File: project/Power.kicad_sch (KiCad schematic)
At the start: 20 parts, among them IC101 nPM1300-QEXX, X101 BATTERY

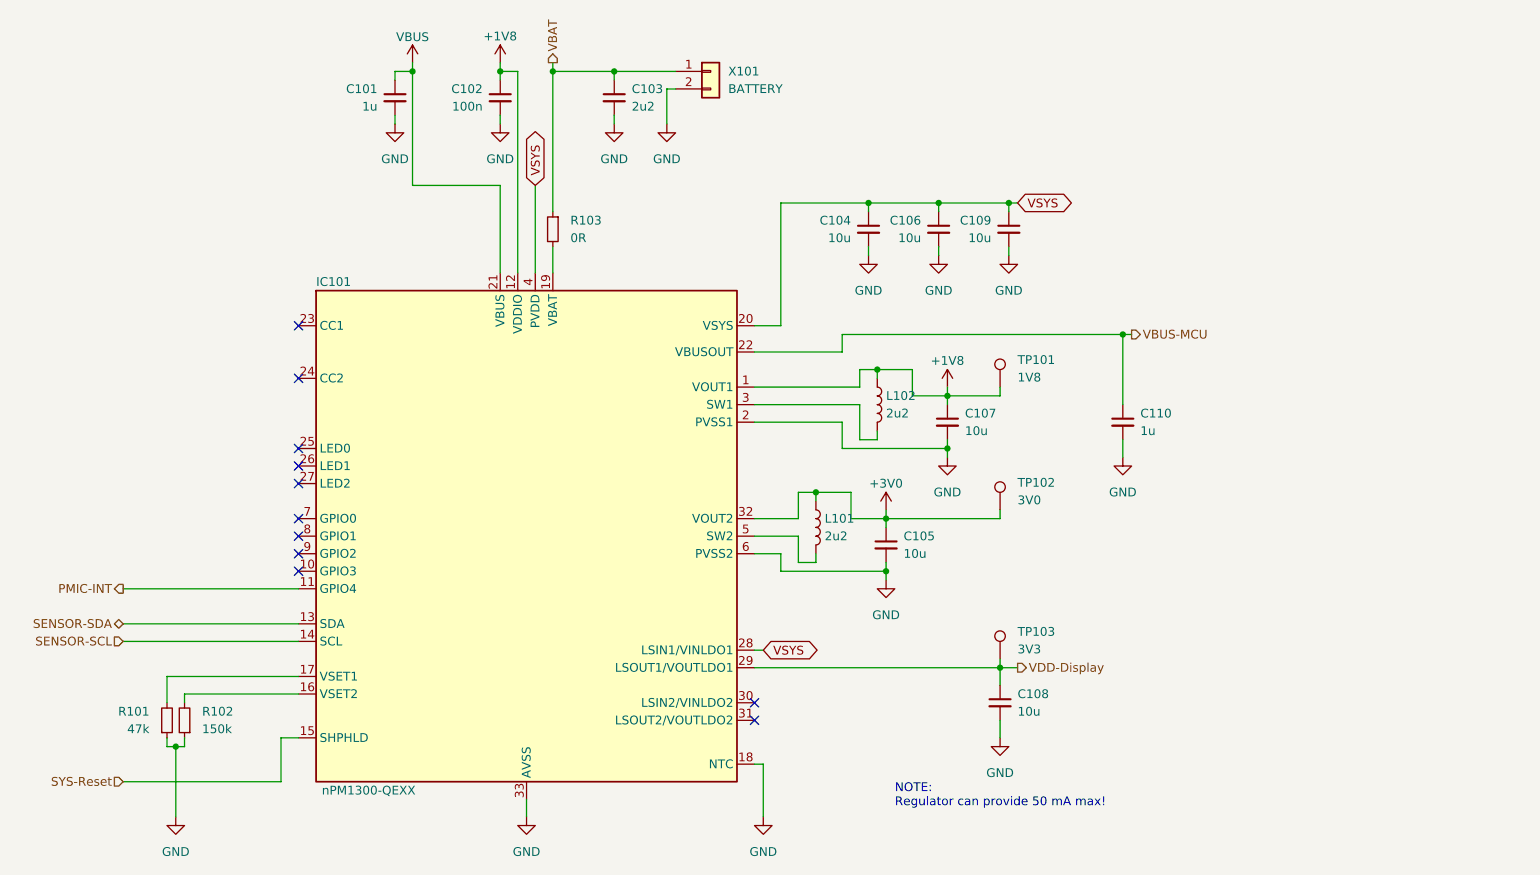
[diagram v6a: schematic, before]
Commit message: Update library paths, fix wrong supply voltage for vibration motor (VSys instead VBusOut)
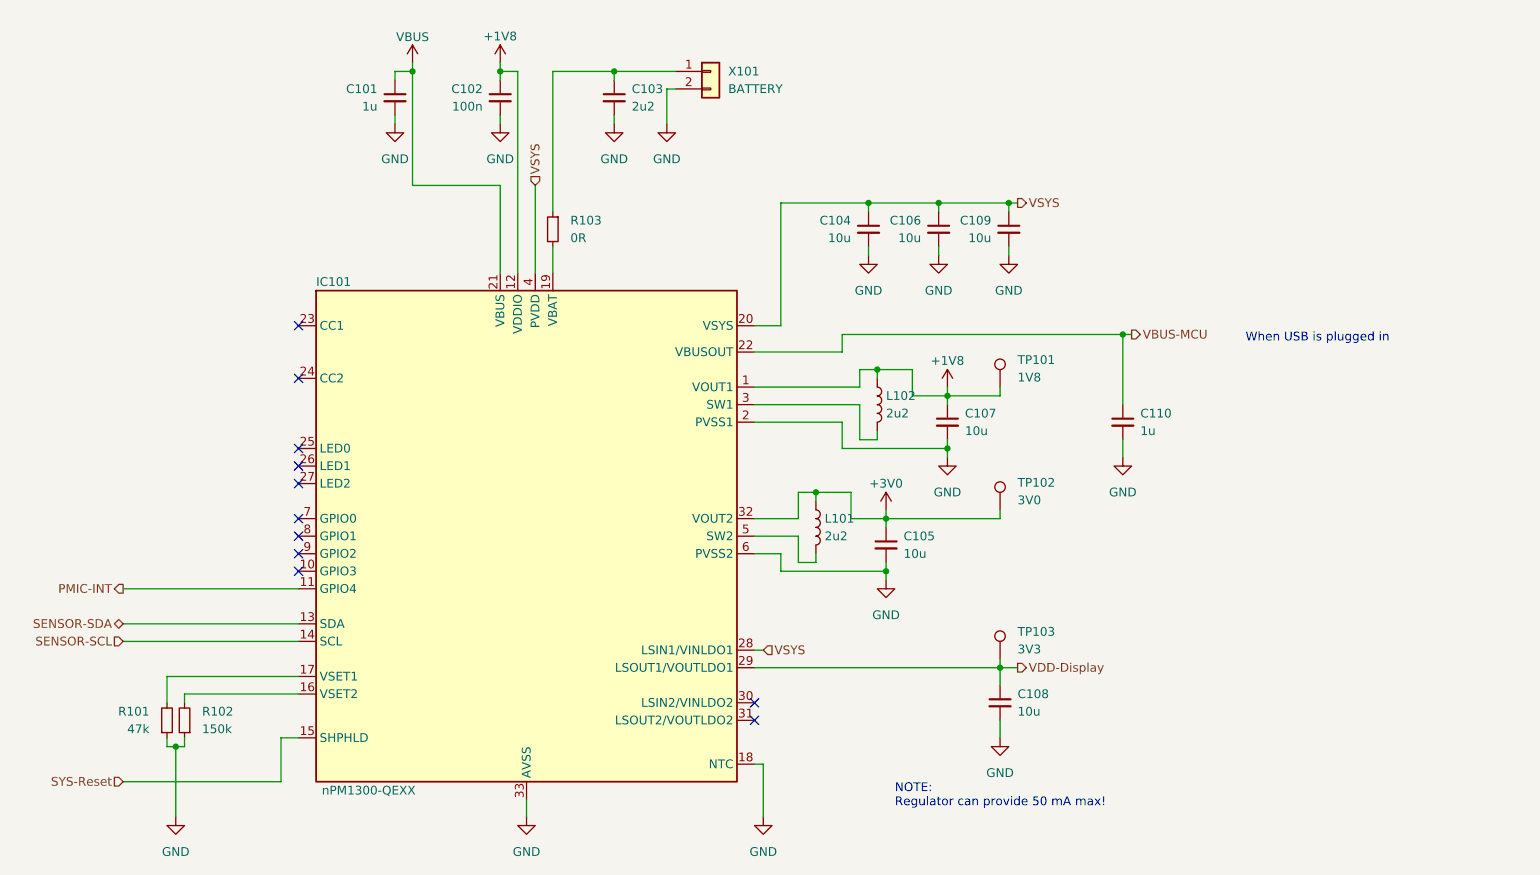
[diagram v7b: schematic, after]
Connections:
- net VBAT: no longer names the net of C103.1, R103.1, X101.1 (Pin_1)
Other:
- note added: "When USB is plugged in"
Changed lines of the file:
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@@
   (junction (at 181.61 59.69) (diameter 0) (color 0 0 0 0)
-  )
-  (junction (at 135.89 40.64) (diameter 0) (color 0 0 0 0)
   )
   (junction (at 182.88 83.82) (diameter 0) (color 0 0 0 0)
@@
     (stroke (width 0) (type default))
   )
-  (wire (pts (xy 135.89 39.37) (xy 135.89 40.64))
-    (stroke (width 0) (type default))
-  )
   (wire (pts (xy 182.88 83.82) (xy 187.96 83.82))
     (stroke (width 0) (type default))
@@
   (wire (pts (xy 133.35 69.85) (xy 133.35 57.15))
     (stroke (width 0) (type default))
+  )
+  (text "When USB is plugged in" (at 236.22 80.01 0)
+    (effects (font (size 1.27 1.27)) (justify left bottom))
   )
   (text "NOTE:\nRegulator can provide 50 mA max!" (at 185.42 147.32 0)
     (effects (font (size 1.27 1.27)) (justify left bottom))
   )
-  (global_label "VSYS" (shape bidirectional) (at 166.37 124.46 0) (fields_autoplaced)
-    (effects (font (size 1.27 1.27)) (justify left))
-    (property "Intersheetrefs" "${INTERSHEET_REFS}" (at 174.9833 124.46 0)
-      (effects (font (size 1.27 1.27)) (justify left) hide)
-    )
-  )
-  (global_label "VSYS" (shape bidirectional) (at 133.35 57.15 90) (fields_autoplaced)
-    (effects (font (size 1.27 1.27)) (justify left))
-    (property "Intersheetrefs" "${INTERSHEET_REFS}" (at 133.35 48.5367 90)
-      (effects (font (size 1.27 1.27)) (justify left) hide)
-    )
-  )
-  (global_label "VSYS" (shape bidirectional) (at 203.2 59.69 0) (fields_autoplaced)
-    (effects (font (size 1.27 1.27)) (justify left))
-    (property "Intersheetrefs" "${INTERSHEET_REFS}" (at 211.8133 59.69 0)
-      (effects (font (size 1.27 1.27)) (justify left) hide)
-    )
+  (hierarchical_label "VSYS" (shape output) (at 203.2 59.69 0) (fields_autoplaced)
+    (effects (font (size 1.27 1.27)) (justify left))
   )
   (hierarchical_label "VBUS-MCU" (shape output) (at 219.71 78.74 0) (fields_autoplaced)
@@
     (effects (font (size 1.27 1.27)) (justify right))
   )
+  (hierarchical_label "VSYS" (shape input) (at 166.37 124.46 0) (fields_autoplaced)
+    (effects (font (size 1.27 1.27)) (justify left))
+  )
   (hierarchical_label "VDD-Display" (shape output) (at 203.2 127 0) (fields_autoplaced)
+    (effects (font (size 1.27 1.27)) (justify left))
+  )
+  (hierarchical_label "VSYS" (shape input) (at 133.35 57.15 90) (fields_autoplaced)
     (effects (font (size 1.27 1.27)) (justify left))
   )
@@
     (effects (font (size 1.27 1.27)) (justify right))
   )
-  (hierarchical_label "VBAT" (shape output) (at 135.89 39.37 90) (fields_autoplaced)
-    (effects (font (size 1.27 1.27)) (justify left))
-  )
   (hierarchical_label "PMIC-INT" (shape output) (at 73.66 115.57 180) (fields_autoplaced)

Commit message: - Replace flash with MX25L51245GZ2I - Replace bridge resistors for SWD / USB switch with jumpers - Fix missing datasheets, update documentation - Fix wrong reset label at the dock connector - Add new logo
Signed-off-by: Daniel Kampert <DanielKampert@kampis-elektroecke.de>
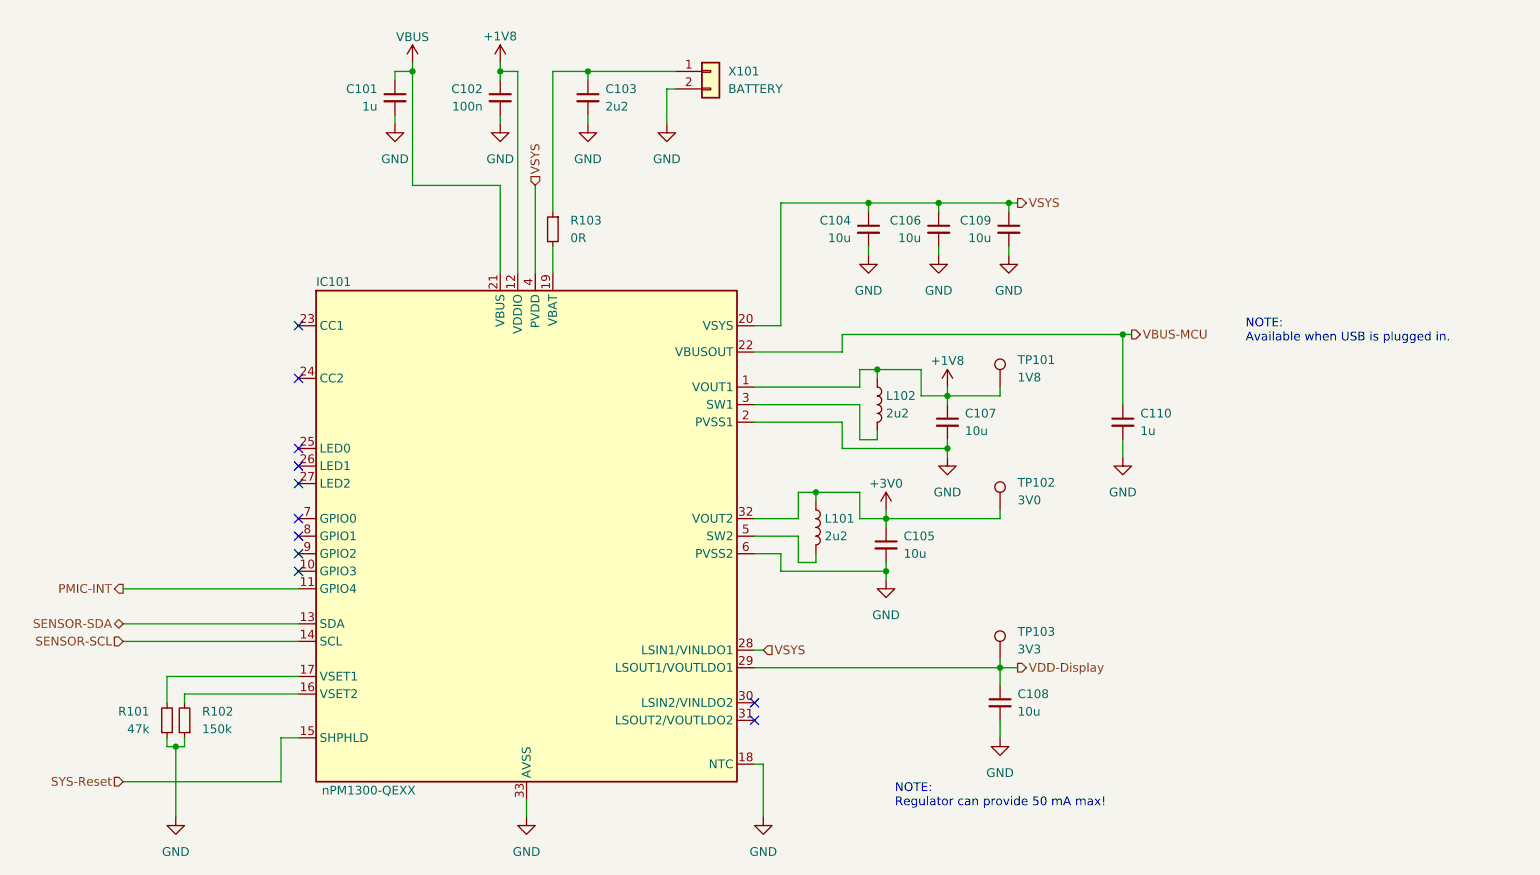
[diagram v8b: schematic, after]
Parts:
- R103: now in the parts list
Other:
- note added: "NOTE: Available when USB is plugged in."
- note removed: "When USB is plugged in"
- moved on the sheet: C103
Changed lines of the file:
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@@
   (junction (at 81.28 138.43) (diameter 0) (color 0 0 0 0)
   )
-  (junction (at 144.78 40.64) (diameter 0) (color 0 0 0 0)
+  (junction (at 140.97 40.64) (diameter 0) (color 0 0 0 0)
   )
   (junction (at 193.04 95.25) (diameter 0) (color 0 0 0 0)
@@
     (stroke (width 0) (type default))
   )
-  (wire (pts (xy 179.07 101.6) (xy 179.07 105.41))
+  (wire (pts (xy 180.34 101.6) (xy 180.34 105.41))
     (stroke (width 0) (type default))
   )
@@
     (stroke (width 0) (type default))
   )
-  (wire (pts (xy 144.78 40.64) (xy 144.78 41.91))
+  (wire (pts (xy 140.97 40.64) (xy 140.97 41.91))
     (stroke (width 0) (type default))
   )
@@
     (stroke (width 0) (type default))
   )
-  (wire (pts (xy 187.96 83.82) (xy 187.96 87.63))
+  (wire (pts (xy 189.23 83.82) (xy 189.23 87.63))
     (stroke (width 0) (type default))
   )
@@
     (stroke (width 0) (type default))
   )
-  (wire (pts (xy 135.89 40.64) (xy 144.78 40.64))
+  (wire (pts (xy 135.89 40.64) (xy 140.97 40.64))
     (stroke (width 0) (type default))
   )
@@
     (stroke (width 0) (type default))
   )
-  (wire (pts (xy 179.07 105.41) (xy 184.15 105.41))
+  (wire (pts (xy 180.34 105.41) (xy 184.15 105.41))
     (stroke (width 0) (type default))
   )
@@
     (stroke (width 0) (type default))
   )
-  (wire (pts (xy 173.99 101.6) (xy 179.07 101.6))
+  (wire (pts (xy 173.99 101.6) (xy 180.34 101.6))
     (stroke (width 0) (type default))
   )
@@
     (stroke (width 0) (type default))
   )
-  (wire (pts (xy 187.96 87.63) (xy 193.04 87.63))
+  (wire (pts (xy 189.23 87.63) (xy 193.04 87.63))
     (stroke (width 0) (type default))
   )
@@
     (stroke (width 0) (type default))
   )
-  (wire (pts (xy 144.78 40.64) (xy 153.67 40.64))
+  (wire (pts (xy 140.97 40.64) (xy 153.67 40.64))
     (stroke (width 0) (type default))
   )
@@
     (stroke (width 0) (type default))
   )
-  (wire (pts (xy 144.78 46.99) (xy 144.78 48.26))
+  (wire (pts (xy 140.97 46.99) (xy 140.97 48.26))
     (stroke (width 0) (type default))
   )
@@
     (stroke (width 0) (type default))
   )
-  (wire (pts (xy 182.88 83.82) (xy 187.96 83.82))
+  (wire (pts (xy 182.88 83.82) (xy 189.23 83.82))
     (stroke (width 0) (type default))
   )
@@
     (stroke (width 0) (type default))
   )
-  (text "When USB is plugged in" (at 236.22 80.01 0)
+  (text "NOTE:\nAvailable when USB is plugged in." (at 236.22 80.01 0)
     (effects (font (size 1.27 1.27)) (justify left bottom))
   )
@@
       (effects (font (size 1.27 1.27)) hide)
     )
-    (property "Datasheet" "~" (at 158.75 40.64 0)
+    (property "Datasheet" "https://www.molex.com/en-us/products/part-detail/781710002?display=pdf" (at 158.75 40.64 0)
       (effects (font (size 1.27 1.27)) hide)
     )
@@
   )
   (symbol (lib_id "Device:R_Small") (at 135.89 63.5 0) (mirror y) (unit 1)
-    (in_bom no) (on_board yes) (dnp no) (fields_autoplaced)
+    (in_bom yes) (on_board yes) (dnp no) (fields_autoplaced)
     (property "Reference" "R103" (at 138.43 62.23 0)
       (effects (font (size 1.27 1.27)) (justify right))
@@
     )
   )
-  (symbol (lib_id "Device:C_Small") (at 144.78 44.45 0) (mirror y) (unit 1)
-    (in_bom yes) (on_board yes) (dnp no) (fields_autoplaced)
-    (property "Reference" "C103" (at 147.32 43.1863 0)
-      (effects (font (size 1.27 1.27)) (justify right))
-    )
-    (property "Value" "2u2" (at 147.32 45.7263 0)
-      (effects (font (size 1.27 1.27)) (justify right))
-    )
-    (property "Footprint" "Capacitor_SMD:C_0603_1608Metric" (at 144.78 44.45 0)
-      (effects (font (size 1.27 1.27)) hide)
-    )
-    (property "Datasheet" "~" (at 144.78 44.45 0)
-      (effects (font (size 1.27 1.27)) hide)
-    )
-    (property "Mfr." "KYOCERA AVX" (at 144.78 44.45 0)
-      (effects (font (size 1.27 1.27)) hide)
-    )
-    (property "Mfr. No." "06036D225KAT2A" (at 144.78 44.45 0)
-      (effects (font (size 1.27 1.27)) hide)
-    )
-    (property "Distributor" "Mouser" (at 144.78 44.45 0)
-      (effects (font (size 1.27 1.27)) hide)
-    )
-    (property "Order Number" "581-06036D225KAT2A" (at 144.78 44.45 0)
-      (effects (font (size 1.27 1.27)) hide)
-    )
-    (property "CONFIG" "" (at 144.78 44.45 0)
+  (symbol (lib_id "Device:C_Small") (at 140.97 44.45 0) (mirror y) (unit 1)
+    (in_bom yes) (on_board yes) (dnp no) (fields_autoplaced)
+    (property "Reference" "C103" (at 143.51 43.1863 0)
+      (effects (font (size 1.27 1.27)) (justify right))
+    )
+    (property "Value" "2u2" (at 143.51 45.7263 0)
+      (effects (font (size 1.27 1.27)) (justify right))
+    )
+    (property "Footprint" "Capacitor_SMD:C_0603_1608Metric" (at 140.97 44.45 0)
+      (effects (font (size 1.27 1.27)) hide)
+    )
+    (property "Datasheet" "~" (at 140.97 44.45 0)
+      (effects (font (size 1.27 1.27)) hide)
+    )
+    (property "Mfr." "KYOCERA AVX" (at 140.97 44.45 0)
+      (effects (font (size 1.27 1.27)) hide)
+    )
+    (property "Mfr. No." "06036D225KAT2A" (at 140.97 44.45 0)
+      (effects (font (size 1.27 1.27)) hide)
+    )
+    (property "Distributor" "Mouser" (at 140.97 44.45 0)
+      (effects (font (size 1.27 1.27)) hide)
+    )
+    (property "Order Number" "581-06036D225KAT2A" (at 140.97 44.45 0)
+      (effects (font (size 1.27 1.27)) hide)
+    )
+    (property "CONFIG" "" (at 140.97 44.45 0)
       (effects (font (size 1.27 1.27)) hide)
     )
@@
     )
   )
-  (symbol (lib_id "power:GND") (at 144.78 48.26 0) (unit 1)
+  (symbol (lib_id "power:GND") (at 140.97 48.26 0) (unit 1)
     (in_bom yes) (on_board yes) (dnp no)
-    (property "Reference" "#PWR0107" (at 144.78 54.61 0)
-      (effects (font (size 1.27 1.27)) hide)
-    )
-    (property "Value" "GND" (at 144.78 53.34 0)
-      (effects (font (size 1.27 1.27)))
-    )
-    (property "Footprint" "" (at 144.78 48.26 0)
-      (effects (font (size 1.27 1.27)) hide)
-    )
-    (property "Datasheet" "" (at 144.78 48.26 0)
-      (effects (font (size 1.27 1.27)) hide)
-    )
+    (property "Reference" "#PWR0107" (at 140.97 54.61 0)
+      (effects (font (size 1.27 1.27)) hide)
+    )
+    (property "Value" "GND" (at 140.97 53.34 0)
+      (effects (font (size 1.27 1.27)))
+    )
+    (property "Footprint" "" (at 140.97 48.26 0)
+      (effects (font (size 1.27 1.27)) hide)
+    )
+    (property "Datasheet" "" (at 140.97 48.26 0)
+      (effects (font (size 1.27 1.27)) hide)
+    )
